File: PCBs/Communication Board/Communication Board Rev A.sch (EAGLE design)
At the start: 20 parts

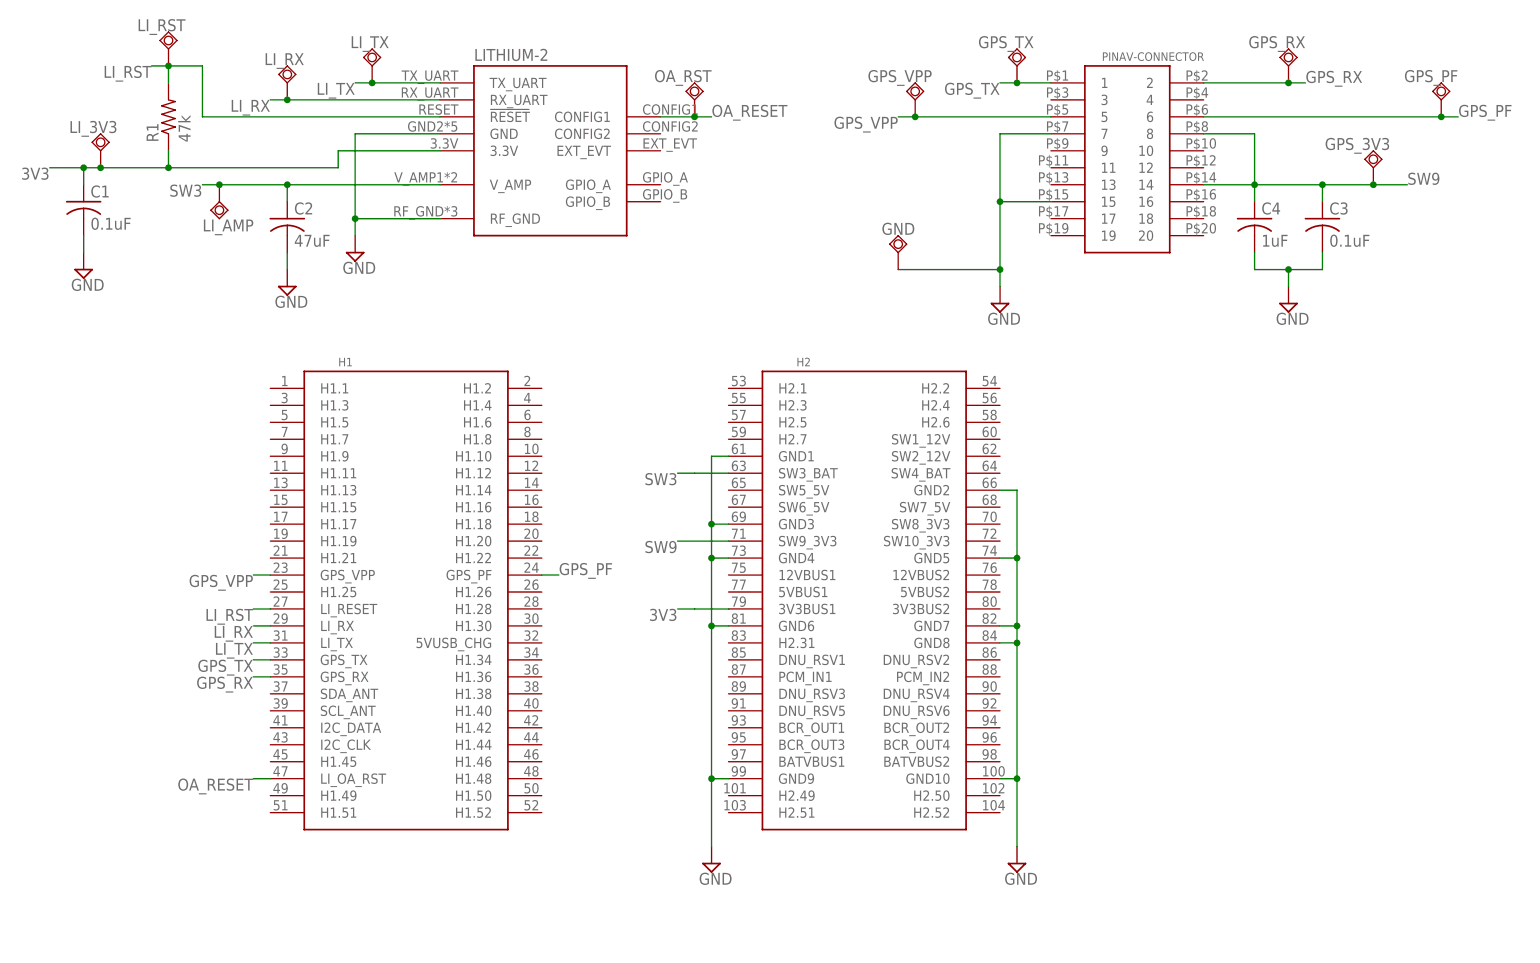
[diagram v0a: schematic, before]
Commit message: Thermally couple radio to chassis
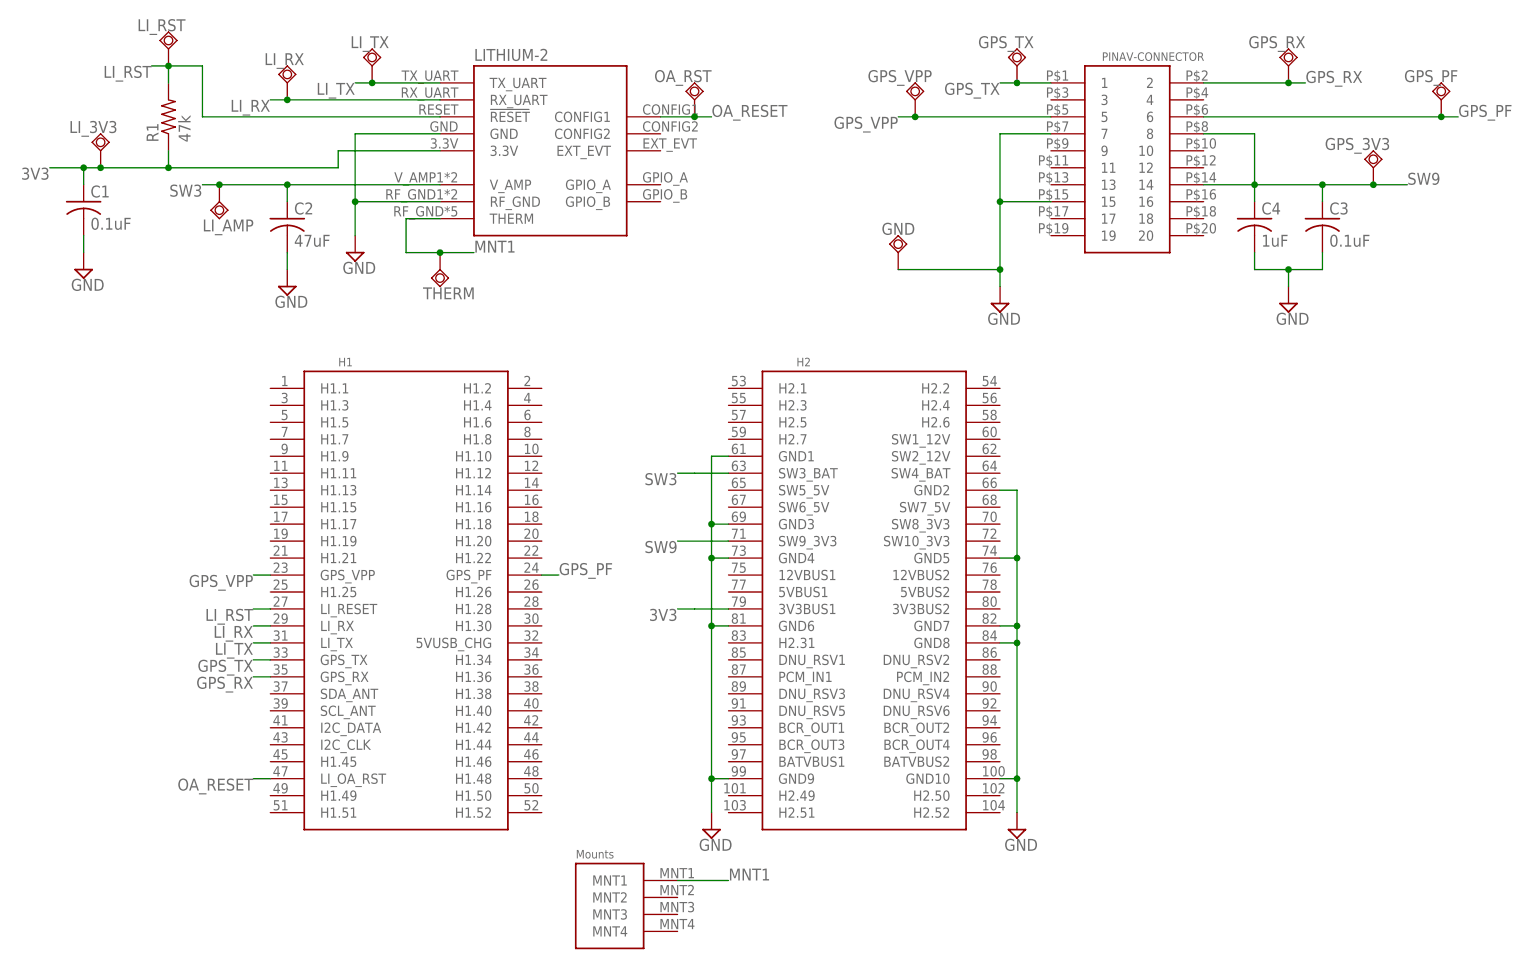
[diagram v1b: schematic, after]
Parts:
- added THERM: TPSQTP20SQ, testpad:TPSQTP20SQ
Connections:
- new net MNT1: LITHIUM-2.THERM, THERM.TP, U$1.MNT1
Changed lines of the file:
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@@
 <part name="LI_RST" library="testpad" library_urn="urn:adsk.eagle:library:385" deviceset="TPSQ" device="TP10SQ" package3d_urn="urn:adsk.eagle:package:27962/1"/>
 <part name="R1" library="resistor" library_urn="urn:adsk.eagle:library:348" deviceset="R-US_" device="R0805" package3d_urn="urn:adsk.eagle:package:23553/2" value="47k"/>
+<part name="THERM" library="testpad" library_urn="urn:adsk.eagle:library:385" deviceset="TPSQ" device="TP20SQ" package3d_urn="urn:adsk.eagle:package:27980/1"/>
 </parts>
 <sheets>
@@
 <instance part="SUPPLY1" gate="GND" x="-5.08" y="48.26"/>
 <instance part="SUPPLY2" gate="GND" x="35.56" y="50.8"/>
-<instance part="SUPPLY5" gate="GND" x="88.9" y="-40.64"/>
-<instance part="SUPPLY6" gate="GND" x="134.62" y="-40.64"/>
+<instance part="SUPPLY5" gate="GND" x="88.9" y="-35.56"/>
+<instance part="SUPPLY6" gate="GND" x="134.62" y="-35.56"/>
 <instance part="C2" gate="G$1" x="25.4" y="55.88"/>
 <instance part="SUPPLY7" gate="GND" x="25.4" y="45.72"/>
@@
 <instance part="LI_RST" gate="G$1" x="7.62" y="81.28" rot="R180"/>
 <instance part="R1" gate="G$1" x="7.62" y="71.12" rot="R90"/>
+<instance part="THERM" gate="G$1" x="48.26" y="48.26"/>
 </instances>
 <busses>
@@
 </segment>
 <segment>
-<wire x1="48.26" y1="55.88" x2="35.56" y2="55.88" width="0.1524" layer="91"/>
+<wire x1="48.26" y1="58.42" x2="35.56" y2="58.42" width="0.1524" layer="91"/>
 <wire x1="48.26" y1="68.58" x2="35.56" y2="68.58" width="0.1524" layer="91"/>
-<wire x1="35.56" y1="68.58" x2="35.56" y2="55.88" width="0.1524" layer="91"/>
+<wire x1="35.56" y1="68.58" x2="35.56" y2="58.42" width="0.1524" layer="91"/>
 <pinref part="SUPPLY2" gate="GND" pin="GND"/>
-<wire x1="35.56" y1="55.88" x2="35.56" y2="53.34" width="0.1524" layer="91"/>
-<junction x="35.56" y="55.88"/>
+<wire x1="35.56" y1="58.42" x2="35.56" y2="53.34" width="0.1524" layer="91"/>
+<junction x="35.56" y="58.42"/>
 <pinref part="LITHIUM-2" gate="G$1" pin="GND"/>
 <pinref part="LITHIUM-2" gate="G$1" pin="RF_GND"/>
@@
 <wire x1="88.9" y1="-5.08" x2="88.9" y2="-27.94" width="0.1524" layer="91"/>
 <junction x="88.9" y="-5.08"/>
-<wire x1="88.9" y1="-27.94" x2="88.9" y2="-38.1" width="0.1524" layer="91"/>
+<wire x1="88.9" y1="-27.94" x2="88.9" y2="-33.02" width="0.1524" layer="91"/>
 <junction x="88.9" y="-27.94"/>
 <pinref part="SUPPLY5" gate="GND" pin="GND"/>
@@
 <wire x1="134.62" y1="-7.62" x2="134.62" y2="-27.94" width="0.1524" layer="91"/>
 <junction x="134.62" y="-7.62"/>
-<wire x1="134.62" y1="-27.94" x2="134.62" y2="-38.1" width="0.1524" layer="91"/>
+<wire x1="134.62" y1="-27.94" x2="134.62" y2="-33.02" width="0.1524" layer="91"/>
 <junction x="134.62" y="-27.94"/>
 <pinref part="SUPPLY6" gate="GND" pin="GND"/>
@@
 </segment>
 </net>
+<net name="MNT1" class="0">
+<segment>
+<pinref part="LITHIUM-2" gate="G$1" pin="THERM"/>
+<wire x1="48.26" y1="55.88" x2="43.18" y2="55.88" width="0.1524" layer="91"/>
+<wire x1="43.18" y1="55.88" x2="43.18" y2="50.8" width="0.1524" layer="91"/>
+<label x="53.34" y="50.8" size="1.778" layer="95"/>
+<wire x1="43.18" y1="50.8" x2="48.26" y2="50.8" width="0.1524" layer="91"/>
+<pinref part="THERM" gate="G$1" pin="TP"/>
+<wire x1="48.26" y1="50.8" x2="53.34" y2="50.8" width="0.1524" layer="91"/>
+<junction x="48.26" y="50.8"/>
+</segment>
+<segment>
+<pinref part="U$1" gate="A" pin="MNT1"/>
+<wire x1="83.82" y1="-43.18" x2="91.44" y2="-43.18" width="0.1524" layer="91"/>
+<label x="91.44" y="-43.18" size="1.778" layer="95"/>
+</segment>
+</net>

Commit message: Create comm parts list
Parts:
- removed THERM: TPSQTP20SQ, testpad:TPSQTP20SQ
- added R2: 0, resistor:R-US_R0805
- C2: value 47uF -> 10uF
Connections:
- net GND: now also R2.2
- net MNT1: now also R2.1; no longer THERM.TP
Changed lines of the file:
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@@
 <?xml version="1.0" encoding="utf-8"?>
 <!DOCTYPE eagle SYSTEM "eagle.dtd">
-<eagle version="9.1.1">
+<eagle version="9.1.2">
 <drawing>
 <settings>
@@
 <part name="SUPPLY5" library="supply2" library_urn="urn:adsk.eagle:library:372" deviceset="GND" device=""/>
 <part name="SUPPLY6" library="supply2" library_urn="urn:adsk.eagle:library:372" deviceset="GND" device=""/>
-<part name="C2" library="resistor" library_urn="urn:adsk.eagle:library:348" deviceset="C-US" device="C0805" package3d_urn="urn:adsk.eagle:package:23617/2" value="47uF"/>
+<part name="C2" library="resistor" library_urn="urn:adsk.eagle:library:348" deviceset="C-US" device="C0805" package3d_urn="urn:adsk.eagle:package:23617/2" value="10uF"/>
 <part name="SUPPLY7" library="supply2" library_urn="urn:adsk.eagle:library:372" deviceset="GND" device=""/>
 <part name="C3" library="resistor" library_urn="urn:adsk.eagle:library:348" deviceset="C-US" device="C0805" package3d_urn="urn:adsk.eagle:package:23617/2" value="0.1uF"/>
@@
 <part name="LI_RST" library="testpad" library_urn="urn:adsk.eagle:library:385" deviceset="TPSQ" device="TP10SQ" package3d_urn="urn:adsk.eagle:package:27962/1"/>
 <part name="R1" library="resistor" library_urn="urn:adsk.eagle:library:348" deviceset="R-US_" device="R0805" package3d_urn="urn:adsk.eagle:package:23553/2" value="47k"/>
-<part name="THERM" library="testpad" library_urn="urn:adsk.eagle:library:385" deviceset="TPSQ" device="TP20SQ" package3d_urn="urn:adsk.eagle:package:27980/1"/>
+<part name="R2" library="resistor" library_urn="urn:adsk.eagle:library:348" deviceset="R-US_" device="R0805" package3d_urn="urn:adsk.eagle:package:23553/2" value="0"/>
 </parts>
 <sheets>
@@
 <instance part="LI_RST" gate="G$1" x="7.62" y="81.28" rot="R180"/>
 <instance part="R1" gate="G$1" x="7.62" y="71.12" rot="R90"/>
-<instance part="THERM" gate="G$1" x="48.26" y="48.26"/>
+<instance part="R2" gate="G$1" x="55.88" y="43.18"/>
 </instances>
 <busses>
@@
 <pinref part="SUPPLY8" gate="GND" pin="GND"/>
 </segment>
+<segment>
+<pinref part="R2" gate="G$1" pin="2"/>
+<wire x1="60.96" y1="43.18" x2="63.5" y2="43.18" width="0.1524" layer="91"/>
+<label x="63.5" y="43.18" size="1.778" layer="95"/>
+</segment>
 </net>
 <net name="GPS_TX" class="0">
@@
 <pinref part="LITHIUM-2" gate="G$1" pin="THERM"/>
 <wire x1="48.26" y1="55.88" x2="43.18" y2="55.88" width="0.1524" layer="91"/>
-<wire x1="43.18" y1="55.88" x2="43.18" y2="50.8" width="0.1524" layer="91"/>
-<label x="53.34" y="50.8" size="1.778" layer="95"/>
-<wire x1="43.18" y1="50.8" x2="48.26" y2="50.8" width="0.1524" layer="91"/>
-<pinref part="THERM" gate="G$1" pin="TP"/>
-<wire x1="48.26" y1="50.8" x2="53.34" y2="50.8" width="0.1524" layer="91"/>
-<junction x="48.26" y="50.8"/>
-</segment>
-<segment>
+<wire x1="43.18" y1="55.88" x2="43.18" y2="48.26" width="0.1524" layer="91"/>
+<label x="53.34" y="48.26" size="1.778" layer="95"/>
+<wire x1="43.18" y1="48.26" x2="48.26" y2="48.26" width="0.1524" layer="91"/>
+<wire x1="48.26" y1="48.26" x2="53.34" y2="48.26" width="0.1524" layer="91"/>
+<wire x1="48.26" y1="48.26" x2="48.26" y2="43.18" width="0.1524" layer="91"/>
+<junction x="48.26" y="48.26"/>
+<wire x1="48.26" y1="43.18" x2="50.8" y2="43.18" width="0.1524" layer="91"/>
+<pinref part="R2" gate="G$1" pin="1"/>
+</segment>
+<segment>
